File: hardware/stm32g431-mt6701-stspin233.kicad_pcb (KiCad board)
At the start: 4 copper layers, 40.1 x 39.8 mm, 90 parts, among them J101 I2C, J102 UART, J103 CANBUS_IN, J104 CANBUS_OUT, J106 CAN TERMINATION, J107 EXT_PWR, J109 MOT_FPC, J110 MOT_FPC2, J201 STDC14, J601 USB_C_Receptacle_USB2.0, Q501 AO3400A, SW201 DFU, SW202 RESET, U101 SN65HVD230, U201 STM32G431, U301 STSPIN233, U401 MT6701, U501 GC9A01, U601 SRV05-4, U701 XC6206, Y201 12MHz

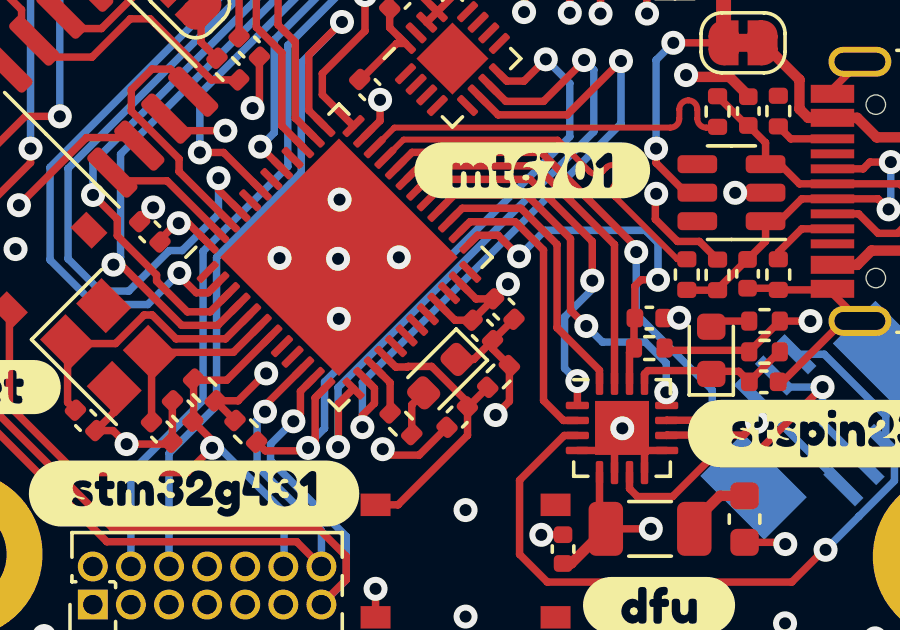
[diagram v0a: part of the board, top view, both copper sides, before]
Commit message: Update with real photos
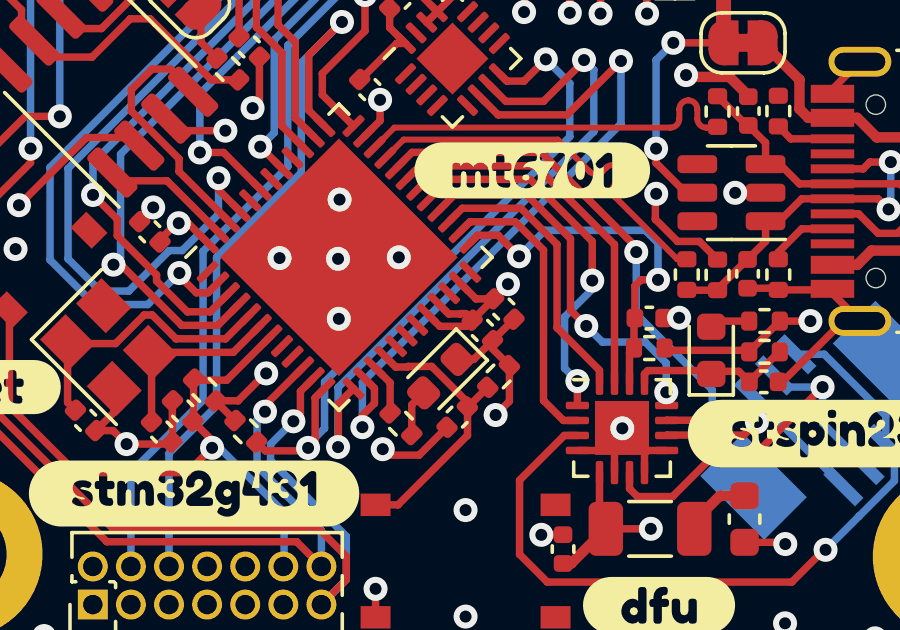
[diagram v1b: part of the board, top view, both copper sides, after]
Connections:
- net /mcu/BOOT0 renamed /mcu/FDCAN1_RX
- J601 pad A6: /mcu/USB_M -> /mcu/USB_P
- J601 pad A7: /mcu/USB_P -> /mcu/USB_M
- J601 pad B6: /mcu/USB_M -> /mcu/USB_P
- J601 pad B7: /mcu/USB_P -> /mcu/USB_M
- U201 pad 20: unconnected-(U201-VREF+-Pad20) -> +3V3
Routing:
- net +3V3: track 49.4 -> 51.1 mm

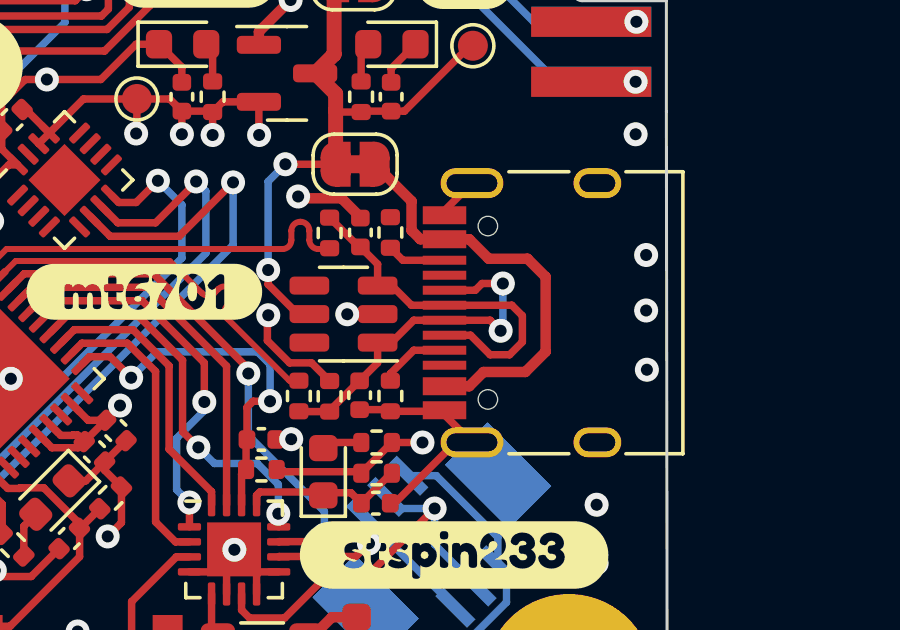
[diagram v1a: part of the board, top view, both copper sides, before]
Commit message: Fix swapped USB pins
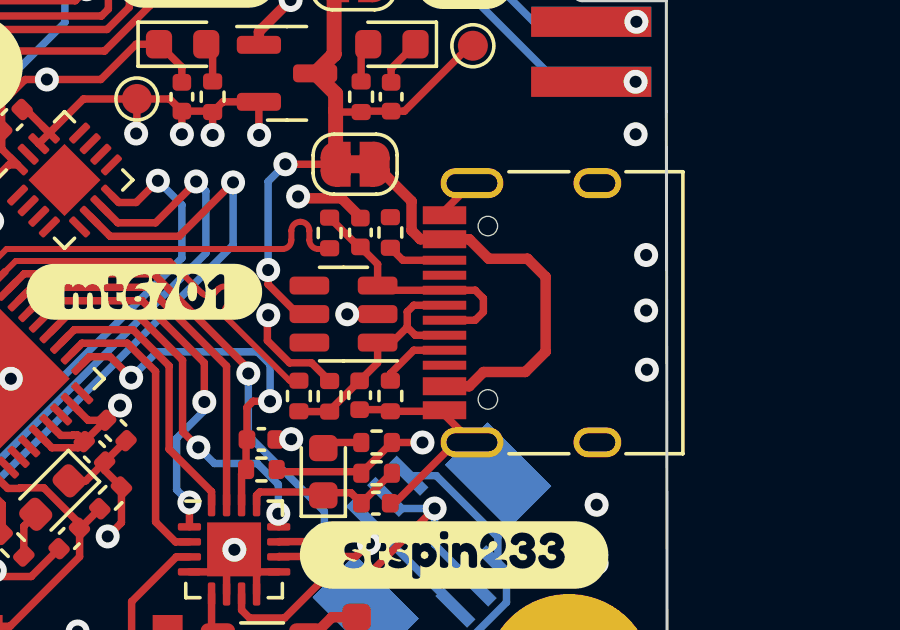
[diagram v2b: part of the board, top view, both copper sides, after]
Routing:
- net /mcu/USB_M: track 12.2 -> 8.40 mm, vias 2 -> 0
- net /mcu/USB_P: track 12.1 -> 8.52 mm
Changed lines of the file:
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@@
   (via (at 110.275 60) (size 0.8) (drill 0.4) (layers "F.Cu" "B.Cu") (net 9))
   (via (at 144.35 57.975) (size 0.8) (drill 0.4) (layers "F.Cu" "B.Cu") (net 9))
-  (segment (start 139.83 71.45) (end 139.175 70.795) (width 0.25) (layer "F.Cu") (net 10))
   (segment (start 138.7 70.08) (end 138.125 69.505) (width 0.25) (layer "F.Cu") (net 10))
-  (segment (start 143.525 72.675) (end 143.1 73.1) (width 0.25) (layer "F.Cu") (net 10))
-  (segment (start 140.93 71.45) (end 139.83 71.45) (width 0.25) (layer "F.Cu") (net 10))
-  (segment (start 141.8 72.45) (end 140.93 72.45) (width 0.25) (layer "F.Cu") (net 10))
-  (segment (start 140.93 71.45) (end 143.175 71.45) (width 0.25) (layer "F.Cu") (net 10))
-  (segment (start 142.45 73.1) (end 141.8 72.45) (width 0.25) (layer "F.Cu") (net 10))
+  (segment (start 140.93 70.95) (end 141.955 70.95) (width 0.25) (layer "F.Cu") (net 10))
+  (segment (start 141.955 70.95) (end 142.225 71.22) (width 0.25) (layer "F.Cu") (net 10))
+  (segment (start 141.95 71.95) (end 140.93 71.95) (width 0.25) (layer "F.Cu") (net 10))
+  (segment (start 138.855 70.95) (end 138.7 70.795) (width 0.25) (layer "F.Cu") (net 10))
+  (segment (start 142.225 71.22) (end 142.225 71.675) (width 0.25) (layer "F.Cu") (net 10))
   (segment (start 138.7 70.795) (end 138.7 70.08) (width 0.25) (layer "F.Cu") (net 10))
-  (segment (start 139.175 70.795) (end 138.7 70.795) (width 0.25) (layer "F.Cu") (net 10))
+  (segment (start 140.93 70.95) (end 138.855 70.95) (width 0.25) (layer "F.Cu") (net 10))
   (segment (start 138.125 69.505) (end 138.075 69.505) (width 0.25) (layer "F.Cu") (net 10))
   (segment (start 138.075 69.505) (end 137.1 68.53) (width 0.25) (layer "F.Cu") (net 10))
-  (segment (start 143.525 71.8) (end 143.525 72.675) (width 0.25) (layer "F.Cu") (net 10))
-  (segment (start 143.1 73.1) (end 142.45 73.1) (width 0.25) (layer "F.Cu") (net 10))
-  (segment (start 143.175 71.45) (end 143.525 71.8) (width 0.25) (layer "F.Cu") (net 10))
-  (segment (start 139.905 71.95) (end 140.93 71.95) (width 0.25) (layer "F.Cu") (net 11))
+  (segment (start 142.225 71.675) (end 141.95 71.95) (width 0.25) (layer "F.Cu") (net 10))
   (segment (start 138.1 73.97) (end 138.092391 73.97) (width 0.25) (layer "F.Cu") (net 11))
   (segment (start 138.7 73.37) (end 138.1 73.97) (width 0.25) (layer "F.Cu") (net 11))
   (segment (start 136.085 74.995) (end 136.075 74.985) (width 0.25) (layer "F.Cu") (net 11))
-  (segment (start 142.8005 72.301) (end 142.4495 71.95) (width 0.25) (layer "F.Cu") (net 11))
-  (segment (start 142.8745 70.725) (end 142.875 70.7255) (width 0.25) (layer "F.Cu") (net 11))
   (segment (start 137.1 74.995) (end 136.085 74.995) (width 0.25) (layer "F.Cu") (net 11))
-  (segment (start 140.93 70.95) (end 141.955 70.95) (width 0.25) (layer "F.Cu") (net 11))
-  (segment (start 142.18 70.725) (end 142.8745 70.725) (width 0.25) (layer "F.Cu") (net 11))
+  (segment (start 139.955 72.45) (end 140.93 72.45) (width 0.25) (layer "F.Cu") (net 11))
+  (segment (start 139.6875 71.6675) (end 139.6875 72.1825) (width 0.25) (layer "F.Cu") (net 11))
+  (segment (start 139.905 71.45) (end 139.6875 71.6675) (width 0.25) (layer "F.Cu") (net 11))
   (segment (start 138.7 72.695) (end 138.7 73.37) (width 0.25) (layer "F.Cu") (net 11))
   (segment (start 137.1 74.962391) (end 137.1 74.995) (width 0.25) (layer "F.Cu") (net 11))
-  (segment (start 141.955 70.95) (end 142.18 70.725) (width 0.25) (layer "F.Cu") (net 11))
-  (segment (start 139.16 72.695) (end 139.905 71.95) (width 0.25) (layer "F.Cu") (net 11))
-  (segment (start 138.7 72.695) (end 139.16 72.695) (width 0.25) (layer "F.Cu") (net 11))
+  (segment (start 140.93 71.45) (end 139.905 71.45) (width 0.25) (layer "F.Cu") (net 11))
+  (segment (start 138.7 72.695) (end 139.175 72.695) (width 0.25) (layer "F.Cu") (net 11))
+  (segment (start 139.175 72.695) (end 139.6875 72.1825) (width 0.25) (layer "F.Cu") (net 11))
   (segment (start 138.092391 73.97) (end 137.1 74.962391) (width 0.25) (layer "F.Cu") (net 11))
-  (segment (start 142.4495 71.95) (end 140.93 71.95) (width 0.25) (layer "F.Cu") (net 11))
-  (via (at 142.875 70.7255) (size 0.8) (drill 0.4) (layers "F.Cu" "B.Cu") (net 11))
-  (via (at 142.8005 72.301) (size 0.8) (drill 0.4) (layers "F.Cu" "B.Cu") (net 11))
-  (segment (start 142.8005 72.301) (end 142.875 72.2265) (width 0.25) (layer "B.Cu") (net 11))
-  (segment (start 142.875 72.2265) (end 142.875 70.7255) (width 0.25) (layer "B.Cu") (net 11))
+  (segment (start 139.6875 72.1825) (end 139.955 72.45) (width 0.25) (layer "F.Cu") (net 11))
   (segment (start 139.595 64.98) (end 141.775 62.8) (width 0.25) (layer "F.Cu") (net 12))
   (segment (start 141.775 62.8) (end 141.875 62.8) (width 0.25) (layer "F.Cu") (net 12))

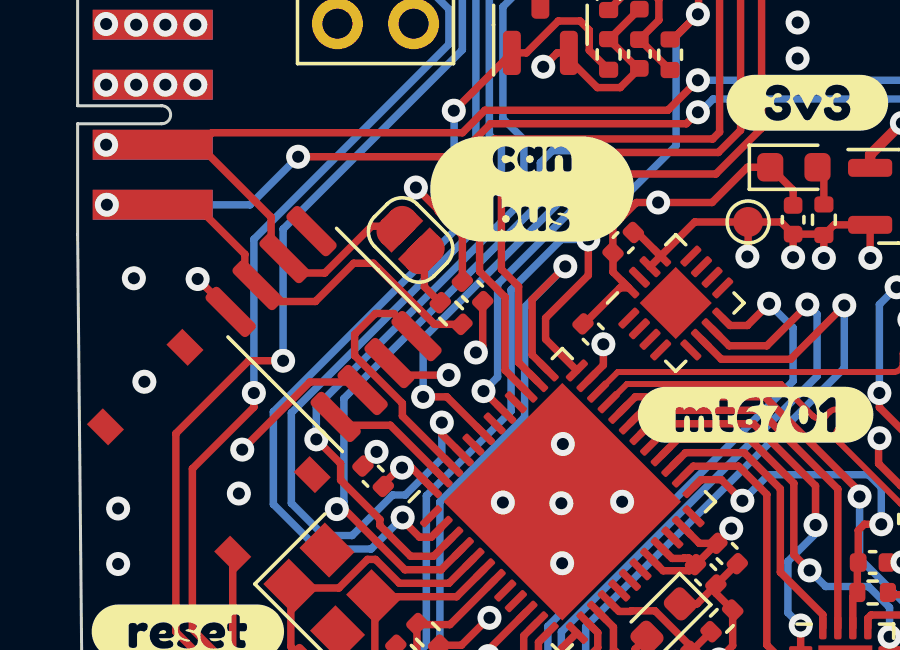
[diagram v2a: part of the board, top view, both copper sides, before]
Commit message: get canbus working
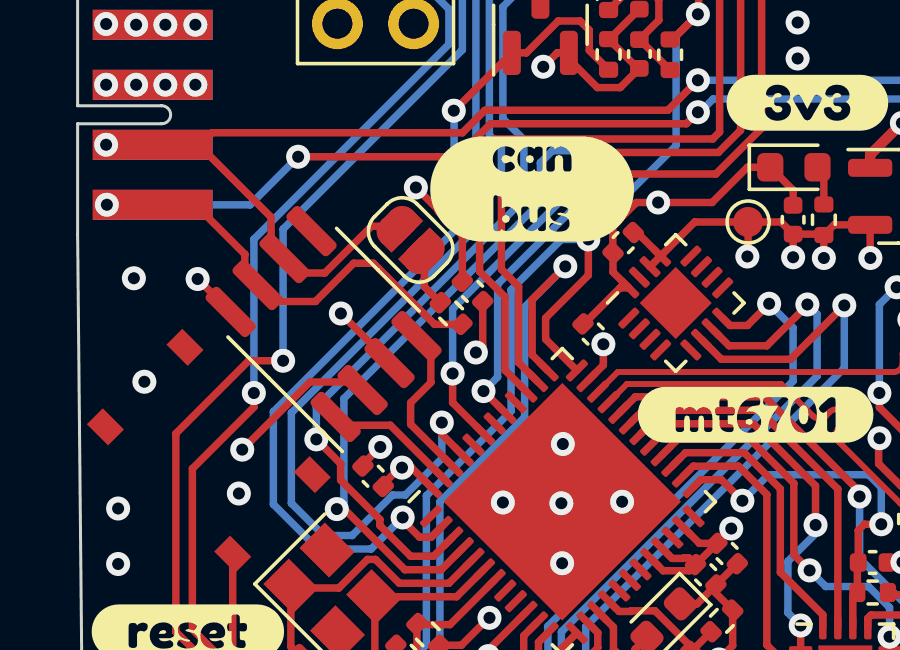
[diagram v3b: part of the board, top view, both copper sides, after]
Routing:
- net /mcu/FDCAN1_RX: track 8.40 -> 5.38 mm
- net /display/TFT_COPI: track 25.2 -> 23.9 mm
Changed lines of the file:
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@@
   (segment (start 128.7 75.775) (end 128.921178 75.996178) (width 0.25) (layer "F.Cu") (net 1))
   (segment (start 126.2 52.975) (end 126.225 53) (width 0.25) (layer "F.Cu") (net 1))
+  (segment (start 118.723026 69.276974) (end 118.723026 69.248026) (width 0.25) (layer "F.Cu") (net 1))
   (segment (start 127.699462 57.845538) (end 127.05 58.495) (width 0.25) (layer "F.Cu") (net 1))
   (segment (start 128.530184 75.788191) (end 128.543375 75.775) (width 0.25) (layer "F.Cu") (net 1))
@@
   (segment (start 125.85 69.346697) (end 125.85 68.65) (width 0.25) (layer "F.Cu") (net 1))
   (segment (start 120.35 64.225305) (end 121.15 65.025305) (width 0.25) (layer "F.Cu") (net 1))
-  (segment (start 120.693201 69.67775) (end 120.691632 69.679319) (width 0.25) (layer "F.Cu") (net 1))
   (segment (start 119.45557 72.762157) (end 120.105366 73.411953) (width 0.25) (layer "F.Cu") (net 1))
   (segment (start 118.514411 73.314411) (end 118.514411 73.389411) (width 0.25) (layer "F.Cu") (net 1))
@@
   (segment (start 133.54 64.67) (end 133.2 65.01) (width 0.25) (layer "F.Cu") (net 1))
   (segment (start 119.6 63.425) (end 120.35 64.175) (width 0.25) (layer "F.Cu") (net 1))
+  (segment (start 118.723026 69.248026) (end 117.100201 67.625201) (width 0.25) (layer "F.Cu") (net 1))
   (segment (start 133.17 64.98) (end 133.2 65.01) (width 0.25) (layer "F.Cu") (net 1))
   (segment (start 127.843161 76.2) (end 128.717356 76.2) (width 0.25) (layer "F.Cu") (net 1))
@@
   (segment (start 126.225 55.695) (end 127.05 56.52) (width 0.25) (layer "F.Cu") (net 1))
   (segment (start 135.41 77) (end 138.105 77) (width 0.25) (layer "F.Cu") (net 1))
-  (segment (start 120.691632 69.679319) (end 119.125371 69.679319) (width 0.25) (layer "F.Cu") (net 1))
   (segment (start 130.071178 74.8349) (end 130.071178 74.85) (width 0.25) (layer "F.Cu") (net 1))
   (segment (start 127.699462 57.161853) (end 127.699462 57.845538) (width 0.25) (layer "F.Cu") (net 1))
@@
   (segment (start 127.405133 66.06408) (end 127.405133 66.064079) (width 0.25) (layer "F.Cu") (net 1))
   (segment (start 125.7 84.95) (end 125.7 85.9) (width 0.25) (layer "F.Cu") (net 1))
-  (segment (start 119.125371 69.679319) (end 118.723026 69.276974) (width 0.25) (layer "F.Cu") (net 1))
   (segment (start 135.335 76.925) (end 135.41 77) (width 0.25) (layer "F.Cu") (net 1))
   (segment (start 138.155 77.045) (end 139.175 76.025) (width 0.25) (layer "F.Cu") (net 1))
@@
   (via (at 125.7 84.95) (size 0.8) (drill 0.4) (layers "F.Cu" "B.Cu") (net 1))
   (via (at 119.6 63.425) (size 0.8) (drill 0.4) (layers "F.Cu" "B.Cu") (net 1))
+  (via (at 117.100201 67.625201) (size 0.8) (drill 0.4) (layers "F.Cu" "B.Cu") (net 1))
   (via (at 126.2 52.975) (size 0.8) (drill 0.4) (layers "F.Cu" "B.Cu") (net 1))
   (via (at 122.054039 77.76962) (size 0.8) (drill 0.4) (layers "F.Cu" "B.Cu") (net 1))
   (via (at 125.85 68.65) (size 0.8) (drill 0.4) (layers "F.Cu" "B.Cu") (net 1))
   (via (at 140.195511 76.025138) (size 0.8) (drill 0.4) (layers "F.Cu" "B.Cu") (net 1))
-  (via (at 120.693201 69.67775) (size 0.8) (drill 0.4) (layers "F.Cu" "B.Cu") (net 1))
   (segment (start 130.65 62.75) (end 129.475 63.925) (width 0.25) (layer "F.Cu") (net 2))
   (segment (start 118.926421 78.687183) (end 118.926421 80.044827) (width 0.25) (layer "F.Cu") (net 2))
   (segment (start 116.375 79.675) (end 116.95 79.675) (width 0.25) (layer "F.Cu") (net 2))
+  (segment (start 117.835589 72.65208) (end 117.835589 72.710589) (width 0.25) (layer "F.Cu") (net 2))
   (segment (start 126.403814 66.771186) (end 126.698026 66.771186) (width 0.25) (layer "F.Cu") (net 2))
   (segment (start 133.165 80.3375) (end 133.915 79.5875) (width 0.25) (layer "F.Cu") (net 2))
   (segment (start 116.95 79.675) (end 117.4 80.125) (width 0.25) (layer "F.Cu") (net 2))
   (segment (start 134.665 80.3375) (end 133.9275 79.6) (width 0.25) (layer "F.Cu") (net 2))
-  (segment (start 118.288178 72.236777) (end 117.835589 72.689366) (width 0.25) (layer "F.Cu") (net 2))
   (segment (start 130.310589 75.964411) (end 129.6 76.675) (width 0.25) (layer "F.Cu") (net 2))
   (segment (start 137.175 81.85) (end 138 81.85) (width 0.35) (layer "F.Cu") (net 2))
@@
   (segment (start 125.203822 67.971178) (end 126.403814 66.771186) (width 0.25) (layer "F.Cu") (net 2))
   (segment (start 125.649462 60.095) (end 126.41 60.095) (width 0.25) (layer "F.Cu") (net 2))
-  (segment (start 117.835589 72.689366) (end 117.835589 72.710589) (width 0.25) (layer "F.Cu") (net 2))
   (segment (start 139.12 78.05) (end 139.265 78.05) (width 0.25) (layer "F.Cu") (net 2))
   (segment (start 126.925 54.5375) (end 127.625 54.5375) (width 0.25) (layer "F.Cu") (net 2))
@@
   (segment (start 130.314411 75.964411) (end 130.310589 75.964411) (width 0.25) (layer "F.Cu") (net 2))
   (segment (start 126.165797 64.711177) (end 126.951974 63.925) (width 0.25) (layer "F.Cu") (net 2))
+  (segment (start 118.41355 72.074119) (end 117.835589 72.65208) (width 0.25) (layer "F.Cu") (net 2))
   (segment (start 121.828822 68.696678) (end 121.828822 67.228822) (width 0.25) (layer "F.Cu") (net 2))
   (segment (start 126.165797 65.598441) (end 126.165797 64.711177) (width 0.25) (layer "F.Cu") (net 2))
@@
   (via (at 125.939193 80.294416) (size 0.8) (drill 0.4) (layers "F.Cu" "B.Cu") (net 2))
   (via (at 146 80.05) (size 0.8) (drill 0.4) (layers "F.Cu" "B.Cu") (free) (net 2))
-  (via (at 118.288178 72.236777) (size 0.8) (drill 0.4) (layers "F.Cu" "B.Cu") (net 2))
+  (via (at 118.41355 72.074119) (size 0.8) (drill 0.4) (layers "F.Cu" "B.Cu") (net 2))
   (via (at 142.2 47.925) (size 0.8) (drill 0.4) (layers "F.Cu" "B.Cu") (free) (net 2))
   (via (at 128.7 82.325) (size 0.8) (drill 0.4) (layers "F.Cu" "B.Cu") (free) (net 2))
@@
   (segment (start 124.65 63.3) (end 124.65 63.156554) (width 0.25) (layer "F.Cu") (net 25))
   (segment (start 125.549195 62.257359) (end 129.681245 62.257359) (width 0.25) (layer "F.Cu") (net 25))
-  (segment (start 120.633266 70.404319) (end 121.873133 71.644186) (width 0.25) (layer "F.Cu") (net 25))
   (segment (start 130.425 61.513604) (end 130.425 54.5375) (width 0.25) (layer "F.Cu") (net 25))
-  (segment (start 119.842851 70.404319) (end 120.633266 70.404319) (width 0.25) (layer "F.Cu") (net 25))
   (segment (start 129.681245 62.257359) (end 130.425 61.513604) (width 0.25) (layer "F.Cu") (net 25))
+  (segment (start 120.825 70.596053) (end 121.873133 71.644186) (width 0.25) (layer "F.Cu") (net 25))
+  (segment (start 120.825 69.625) (end 120.825 70.596053) (width 0.25) (layer "F.Cu") (net 25))
   (via (at 124.65 63.3) (size 0.8) (drill 0.4) (layers "F.Cu" "B.Cu") (net 25))
-  (via (at 119.842851 70.404319) (size 0.8) (drill 0.4) (layers "F.Cu" "B.Cu") (net 25))
-  (segment (start 119.842851 68.452733) (end 119.842851 70.404319) (width 0.25) (layer "B.Cu") (net 25))
-  (segment (start 124.65 63.3) (end 124.65 63.645584) (width 0.25) (layer "B.Cu") (net 25))
-  (segment (start 124.65 63.645584) (end 119.842851 68.452733) (width 0.25) (layer "B.Cu") (net 25))
+  (via (at 120.825 69.625) (size 0.8) (drill 0.4) (layers "F.Cu" "B.Cu") (net 25))
+  (segment (start 124.65 63.645584) (end 124.65 63.3) (width 0.25) (layer "B.Cu") (net 25))
+  (segment (start 120.825 67.470584) (end 124.65 63.645584) (width 0.25) (layer "B.Cu") (net 25))
+  (segment (start 120.825 69.625) (end 120.825 67.470584) (width 0.25) (layer "B.Cu") (net 25))
   (segment (start 123.287346 70.229973) (end 122.575 69.517627) (width 0.25) (layer "F.Cu") (net 26))
   (segment (start 122.218852 61.807359) (end 129.494849 61.807359) (width 0.25) (layer "F.Cu") (net 26))
@@
   (segment (start 120.458919 73.0584) (end 118.750519 71.35) (width 0.25) (layer "F.Cu") (net 49))
   (segment (start 117.203949 71.35) (end 116.926975 71.073026) (width 0.25) (layer "F.Cu") (net 49))
-  (segment (start 117.558597 69.024713) (end 117.558597 68.316403) (width 0.25) (layer "F.Cu") (net 50))
-  (segment (start 118.867103 67.625) (end 119.621052 68.378949) (width 0.25) (layer "F.Cu") (net 50))
-  (segment (start 120.812473 72.704846) (end 119.15 71.042373) (width 0.25) (layer "F.Cu") (net 50))
-  (segment (start 119.15 71.042373) (end 119.15 70.616116) (width 0.25) (layer "F.Cu") (net 50))
-  (segment (start 119.15 70.616116) (end 117.558597 69.024713) (width 0.25) (layer "F.Cu") (net 50))
-  (segment (start 118.25 67.625) (end 118.867103 67.625) (width 0.25) (layer "F.Cu") (net 50))
-  (segment (start 117.558597 68.316403) (end 118.25 67.625) (width 0.25) (layer "F.Cu") (net 50))
+  (segment (start 120.812473 72.704846) (end 119.425 71.317373) (width 0.25) (layer "F.Cu") (net 50))
+  (segment (start 119.425 70.600305) (end 120.1 69.925305) (width 0.25) (layer "F.Cu") (net 50))
+  (segment (start 120.1 68.857897) (end 119.621052 68.378949) (width 0.25) (layer "F.Cu") (net 50))
+  (segment (start 119.425 71.317373) (end 119.425 70.600305) (width 0.25) (layer "F.Cu") (net 50))
+  (segment (start 120.1 69.925305) (end 120.1 68.857897) (width 0.25) (layer "F.Cu") (net 50))
   (segment (start 118.4 74.4875) (end 118.4 74.690297) (width 0.25) (layer "F.Cu") (net 53))
   (segment (start 128.225 56.425) (end 128.325 56.325) (width 0.25) (layer "F.Cu") (net 53))
